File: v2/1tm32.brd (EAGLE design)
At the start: 50.8 x 50.8 mm, 48 parts, among them IC1 STM32L412RBT6P, IC2 BGM240PA32VNN3, IC3 TPS7A0333PYCHR, J2 10118192-0001LF, J3 FTSH-105-01-L-D, J4 20021321-00020C4LF, SW1 LL3301FF065QJ, U2 LD39050PU33R, Y1 8MHz, Y2 32.7KHz

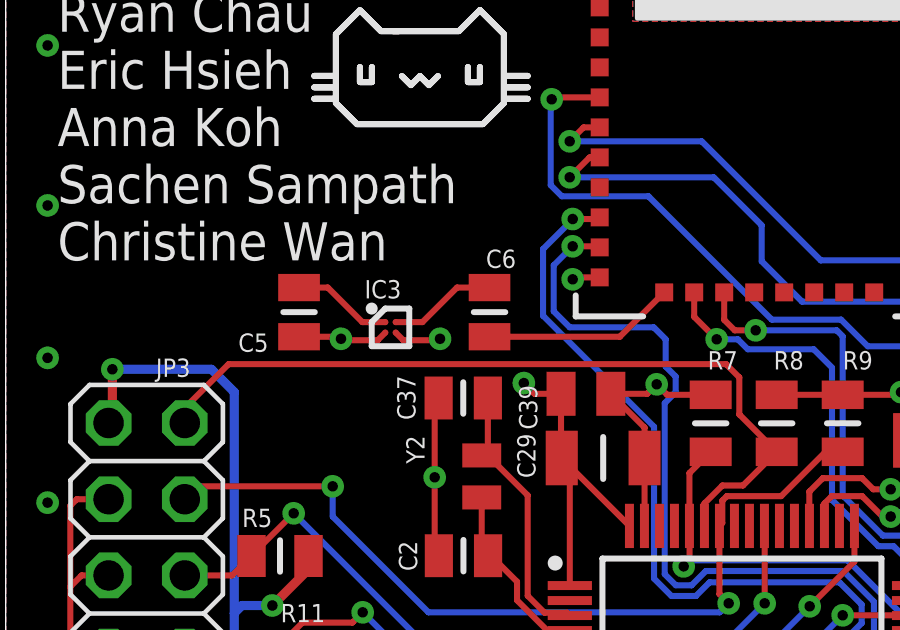
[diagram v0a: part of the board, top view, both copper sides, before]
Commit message: changed voltage regulator
previous one caused clearance issues with the wires
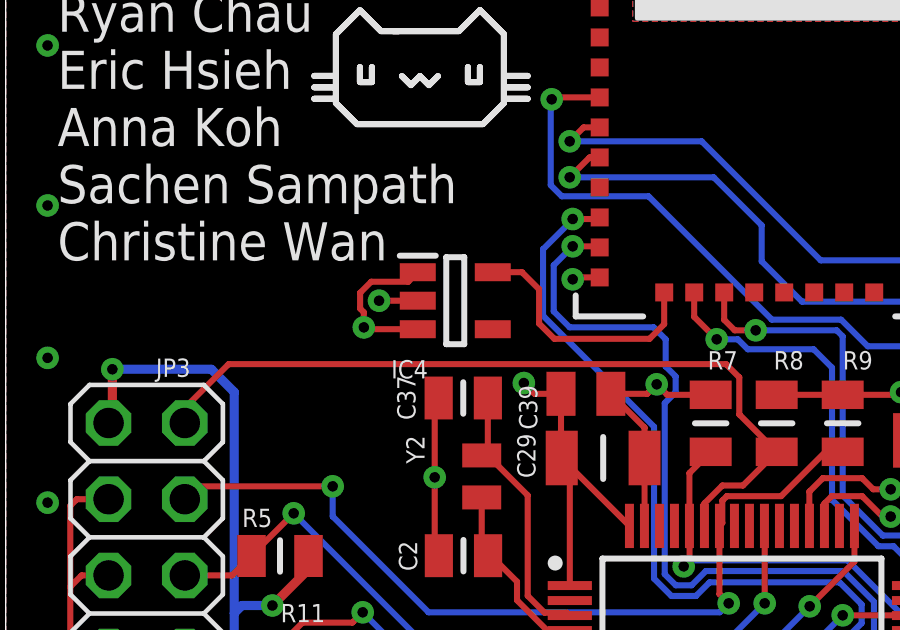
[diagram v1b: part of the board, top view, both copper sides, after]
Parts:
- removed C5, C6: GRM219R61H105KA73D, GRM219R61H105KA73D(1u):CAPC2012X95N
- removed IC3: TPS7A0333PYCHR, TPS7A0333PYCHR(volt_reg):BGA4C35P2X2_64X64X40
- added IC4: TLV73333PQDBVRQ1, TLV73333PQDBVRQ1(volt_reg2):SOT95P280X145-5N
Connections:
- removed net N$1: C6.2, IC3.A2
- removed net N$6: C5.2, IC3.A1
- net 3V3: now also IC4.1, IC4.3; no longer C5.1, IC3.B1
- net GND: now also IC4.2; no longer IC3.B2
- net N$4: now also IC4.5; no longer C6.1
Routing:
- net N$1: track 3.60 -> 0.00 mm
- net N$6: track 3.35 -> 0.00 mm
- net 3V3: track 65.0 -> 67.2 mm
- net N$4: track 6.43 -> 8.56 mm
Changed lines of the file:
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@@
 <attribute name="NAME" x="47.498" y="2.0574" size="0.6096" layer="27" ratio="6" rot="SR90"/>
 </element>
-<element name="IC3" library="TPS7A0333PYCHR(volt_reg)" package="BGA4C35P2X2_64X64X40" value="TPS7A0333PYCHR" x="12.827" y="34.798" smashed="yes">
-<attribute name="DESCRIPTION" value="LDO Voltage Regulators 200-mA, nanopower-IQ (200 nA), low-dropout (LDO) voltage regulator with enable 4-DSBGA -40 to 125" x="12.827" y="34.798" size="1.778" layer="27" display="off"/>
-<attribute name="HEIGHT" value="0.4mm" x="12.827" y="34.798" size="1.778" layer="27" display="off"/>
-<attribute name="MANUFACTURER_NAME" value="Texas Instruments" x="12.827" y="34.798" size="1.778" layer="27" display="off"/>
-<attribute name="MANUFACTURER_PART_NUMBER" value="TPS7A0333PYCHR" x="12.827" y="34.798" size="1.778" layer="27" display="off"/>
-<attribute name="MOUSER_PART_NUMBER" value="595-TPS7A0333PYCHR" x="12.827" y="34.798" size="1.778" layer="27" display="off"/>
-<attribute name="MOUSER_PRICE-STOCK" value="https://www.mouser.co.uk/ProductDetail/Texas-Instruments/TPS7A0333PYCHR?qs=DRkmTr78QASt%252BMCkG4QYQg%3D%3D" x="12.827" y="34.798" size="1.778" layer="27" display="off"/>
-<attribute name="NAME" x="12.573" y="36.068" size="0.6096" layer="25" align="center"/>
-</element>
-<element name="C5" library="GRM219R61H105KA73D(1u)" package="CAPC2012X95N" value="GRM219R61H105KA73D" x="9.779" y="35.306" smashed="yes" rot="R90">
-<attribute name="DESCRIPTION" value="MURATA - GRM219R61H105KA73D - CAP, MLCC, X5R, 1UF, 50V, 0805" x="9.779" y="35.306" size="1.778" layer="27" rot="R90" display="off"/>
-<attribute name="HEIGHT" value="0.95mm" x="9.779" y="35.306" size="1.778" layer="27" rot="R90" display="off"/>
-<attribute name="MANUFACTURER_NAME" value="Murata Electronics" x="9.779" y="35.306" size="1.778" layer="27" rot="R90" display="off"/>
-<attribute name="MANUFACTURER_PART_NUMBER" value="GRM219R61H105KA73D" x="9.779" y="35.306" size="1.778" layer="27" rot="R90" display="off"/>
-<attribute name="MOUSER_PART_NUMBER" value="81-GRM219R61H105KA3D" x="9.779" y="35.306" size="1.778" layer="27" rot="R90" display="off"/>
-<attribute name="MOUSER_PRICE-STOCK" value="https://www.mouser.co.uk/ProductDetail/Murata-Electronics/GRM219R61H105KA73D?qs=O5cugoO6nweiD1nCQ5vS9w%3D%3D" x="9.779" y="35.306" size="1.778" layer="27" rot="R90" display="off"/>
-<attribute name="NAME" x="8.255" y="34.29" size="0.6096" layer="25" rot="R180" align="center"/>
-</element>
-<element name="C6" library="GRM219R61H105KA73D(1u)" package="CAPC2012X95N" value="GRM219R61H105KA73D" x="16.129" y="35.306" smashed="yes" rot="R90">
-<attribute name="DESCRIPTION" value="MURATA - GRM219R61H105KA73D - CAP, MLCC, X5R, 1UF, 50V, 0805" x="16.129" y="35.306" size="1.778" layer="27" rot="R90" display="off"/>
-<attribute name="HEIGHT" value="0.95mm" x="16.129" y="35.306" size="1.778" layer="27" rot="R90" display="off"/>
-<attribute name="MANUFACTURER_NAME" value="Murata Electronics" x="16.129" y="35.306" size="1.778" layer="27" rot="R90" display="off"/>
-<attribute name="MANUFACTURER_PART_NUMBER" value="GRM219R61H105KA73D" x="16.129" y="35.306" size="1.778" layer="27" rot="R90" display="off"/>
-<attribute name="MOUSER_PART_NUMBER" value="81-GRM219R61H105KA3D" x="16.129" y="35.306" size="1.778" layer="27" rot="R90" display="off"/>
-<attribute name="MOUSER_PRICE-STOCK" value="https://www.mouser.co.uk/ProductDetail/Murata-Electronics/GRM219R61H105KA73D?qs=O5cugoO6nweiD1nCQ5vS9w%3D%3D" x="16.129" y="35.306" size="1.778" layer="27" rot="R90" display="off"/>
-<attribute name="NAME" x="16.51" y="37.084" size="0.6096" layer="25" rot="R180" align="center"/>
+<element name="IC4" library="TLV73333PQDBVRQ1(volt_reg2)" package="SOT95P280X145-5N" value="TLV73333PQDBVRQ1" x="14.986" y="35.687" smashed="yes">
+<attribute name="DESCRIPTION" value="Automotive capacitor-free 300-mA LDO regulator with foldback current limit for portable devices" x="14.986" y="35.687" size="1.778" layer="27" display="off"/>
+<attribute name="HEIGHT" value="1.45mm" x="14.986" y="35.687" size="1.778" layer="27" display="off"/>
+<attribute name="MANUFACTURER_NAME" value="Texas Instruments" x="14.986" y="35.687" size="1.778" layer="27" display="off"/>
+<attribute name="MANUFACTURER_PART_NUMBER" value="TLV73333PQDBVRQ1" x="14.986" y="35.687" size="1.778" layer="27" display="off"/>
+<attribute name="MOUSER_PART_NUMBER" value="595-TLV73333PQDBVRQ1" x="14.986" y="35.687" size="1.778" layer="27" display="off"/>
+<attribute name="MOUSER_PRICE-STOCK" value="https://www.mouser.co.uk/ProductDetail/Texas-Instruments/TLV73333PQDBVRQ1?qs=9r4v7xj2LnnYANXVL3PB4Q%3D%3D" x="14.986" y="35.687" size="1.778" layer="27" display="off"/>
+<attribute name="NAME" x="13.462" y="33.401" size="0.6096" layer="25" align="center"/>
 </element>
 </elements>
@@
 <wire x1="28.358" y1="13.118" x2="28.067" y2="12.827" width="0.2032" layer="1"/>
 <via x="28.067" y="12.827" extent="1-16" drill="0.35"/>
-<contactref element="IC3" pad="B2"/>
-<wire x1="14.478" y1="34.417" x2="14.43" y2="34.369" width="0.2032" layer="1"/>
-<wire x1="14.43" y1="34.369" x2="13.256" y2="34.369" width="0.2032" layer="1"/>
-<wire x1="13.002" y1="34.623" x2="13.256" y2="34.369" width="0.2032" layer="1"/>
-<via x="14.478" y="34.417" extent="1-16" drill="0.35"/>
+<contactref element="IC4" pad="2"/>
+<wire x1="13.736" y1="35.687" x2="12.446" y2="35.687" width="0.2032" layer="1"/>
+<via x="12.446" y="35.687" extent="1-16" drill="0.35"/>
 </signal>
 <signal name="BOOT0">
@@
 <wire x1="18.804" y1="30.168" x2="18.536" y2="30.436" width="0.2032" layer="1"/>
 <wire x1="18.804" y1="26.192" x2="18.804" y2="30.168" width="0.2032" layer="1"/>
-<contactref element="IC3" pad="B1"/>
-<contactref element="C5" pad="1"/>
-<wire x1="12.652" y1="34.623" x2="12.398" y2="34.369" width="0.2032" layer="1"/>
-<wire x1="12.398" y1="34.369" x2="11.224" y2="34.369" width="0.2032" layer="1"/>
-<wire x1="11.176" y1="34.417" x2="11.224" y2="34.369" width="0.2032" layer="1"/>
-<via x="11.176" y="34.417" extent="1-16" drill="0.35"/>
-<wire x1="9.779" y1="34.486" x2="11.107" y2="34.486" width="0.2032" layer="1"/>
-<wire x1="11.107" y1="34.486" x2="11.176" y2="34.417" width="0.2032" layer="1"/>
+<contactref element="IC4" pad="3"/>
+<contactref element="IC4" pad="1"/>
+<wire x1="13.736" y1="34.737" x2="11.999" y2="34.737" width="0.2032" layer="1"/>
+<wire x1="11.999" y1="34.737" x2="11.938" y2="34.798" width="0.2032" layer="1"/>
+<via x="11.938" y="34.798" extent="1-16" drill="0.35"/>
+<wire x1="12.18413125" y1="36.3192" x2="11.8138" y2="35.94886875" width="0.2032" layer="1"/>
+<wire x1="11.8138" y1="35.94886875" x2="11.8138" y2="35.42513125" width="0.2032" layer="1"/>
+<wire x1="11.8138" y1="35.42513125" x2="11.938" y2="35.30093125" width="0.2032" layer="1"/>
+<wire x1="11.938" y1="35.30093125" x2="11.938" y2="34.798" width="0.2032" layer="1"/>
+<wire x1="13.736" y1="36.637" x2="13.4182" y2="36.3192" width="0.2032" layer="1"/>
+<wire x1="13.4182" y1="36.3192" x2="12.18413125" y2="36.3192" width="0.2032" layer="1"/>
 </signal>
 <signal name="USART1_RX">
@@
 <signal name="N$4">
 <contactref element="IC2" pad="15"/>
-<contactref element="C6" pad="1"/>
-<wire x1="16.129" y1="34.486" x2="20.472" y2="34.486" width="0.2032" layer="1"/>
-<wire x1="20.472" y1="34.486" x2="21.95" y2="35.964" width="0.2032" layer="1"/>
-</signal>
-<signal name="N$1">
-<contactref element="IC3" pad="A2"/>
-<contactref element="C6" pad="2"/>
-<wire x1="13.002" y1="34.973" x2="13.891" y2="34.973" width="0.2032" layer="1"/>
-<wire x1="15.044" y1="36.126" x2="16.129" y2="36.126" width="0.2032" layer="1"/>
-<wire x1="13.891" y1="34.973" x2="15.044" y2="36.126" width="0.2032" layer="1"/>
-</signal>
-<signal name="N$6">
-<contactref element="IC3" pad="A1"/>
-<contactref element="C5" pad="2"/>
-<wire x1="12.652" y1="34.973" x2="11.89" y2="34.973" width="0.2032" layer="1"/>
-<wire x1="10.737" y1="36.126" x2="9.779" y2="36.126" width="0.2032" layer="1"/>
-<wire x1="11.89" y1="34.973" x2="10.737" y2="36.126" width="0.2032" layer="1"/>
+<contactref element="IC4" pad="5"/>
+<wire x1="21.95" y1="35.964" x2="21.95" y2="34.904" width="0.2032" layer="1"/>
+<wire x1="21.95" y1="34.904" x2="21.463" y2="34.417" width="0.2032" layer="1"/>
+<wire x1="21.463" y1="34.417" x2="18.288" y2="34.417" width="0.2032" layer="1"/>
+<wire x1="17.78" y1="34.925" x2="17.78" y2="36.068" width="0.2032" layer="1"/>
+<wire x1="17.78" y1="36.068" x2="17.211" y2="36.637" width="0.2032" layer="1"/>
+<wire x1="17.211" y1="36.637" x2="16.236" y2="36.637" width="0.2032" layer="1"/>
+<wire x1="18.288" y1="34.417" x2="17.78" y2="34.925" width="0.2032" layer="1"/>
 </signal>
 </signals>
